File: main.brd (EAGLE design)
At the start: 50.8 x 50.8 mm, 54 parts, among them U2 SN65HVD32_D_8

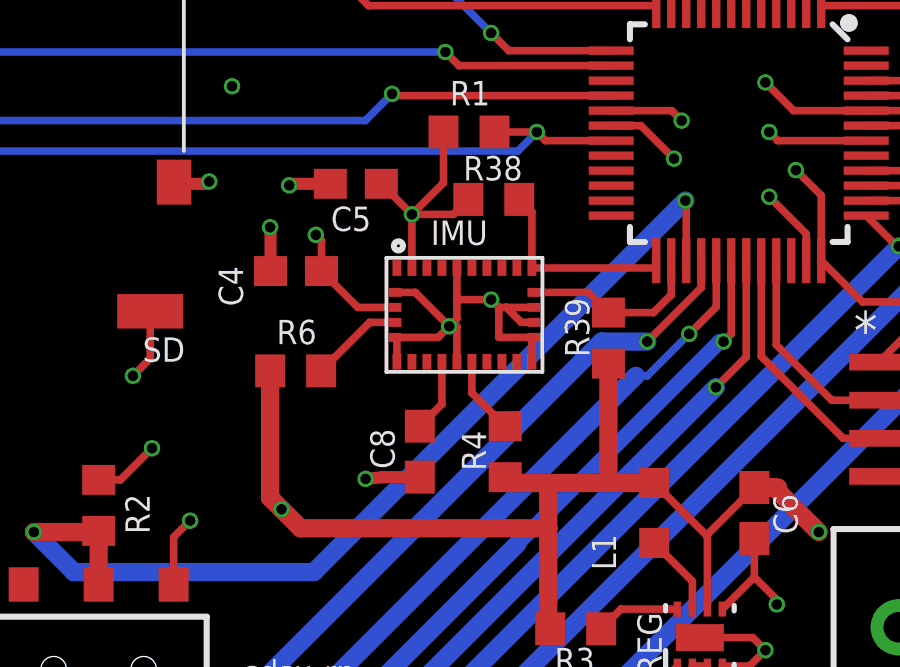
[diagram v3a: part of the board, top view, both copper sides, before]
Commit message: Fixed poly fill not connecting to all pins
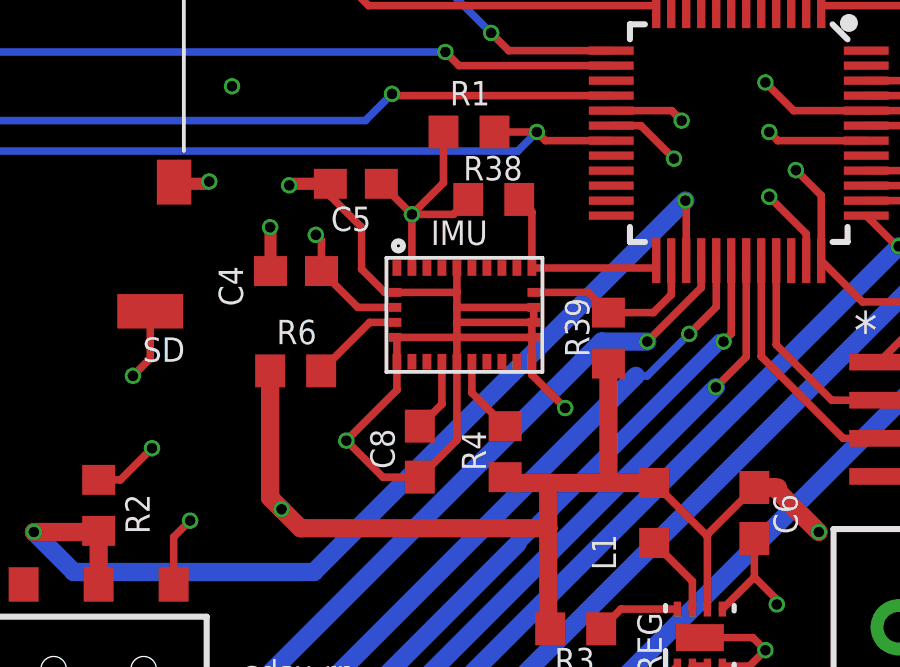
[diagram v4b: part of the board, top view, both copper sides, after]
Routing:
- net GND: track 80.3 -> 98.2 mm, vias 41 -> 40

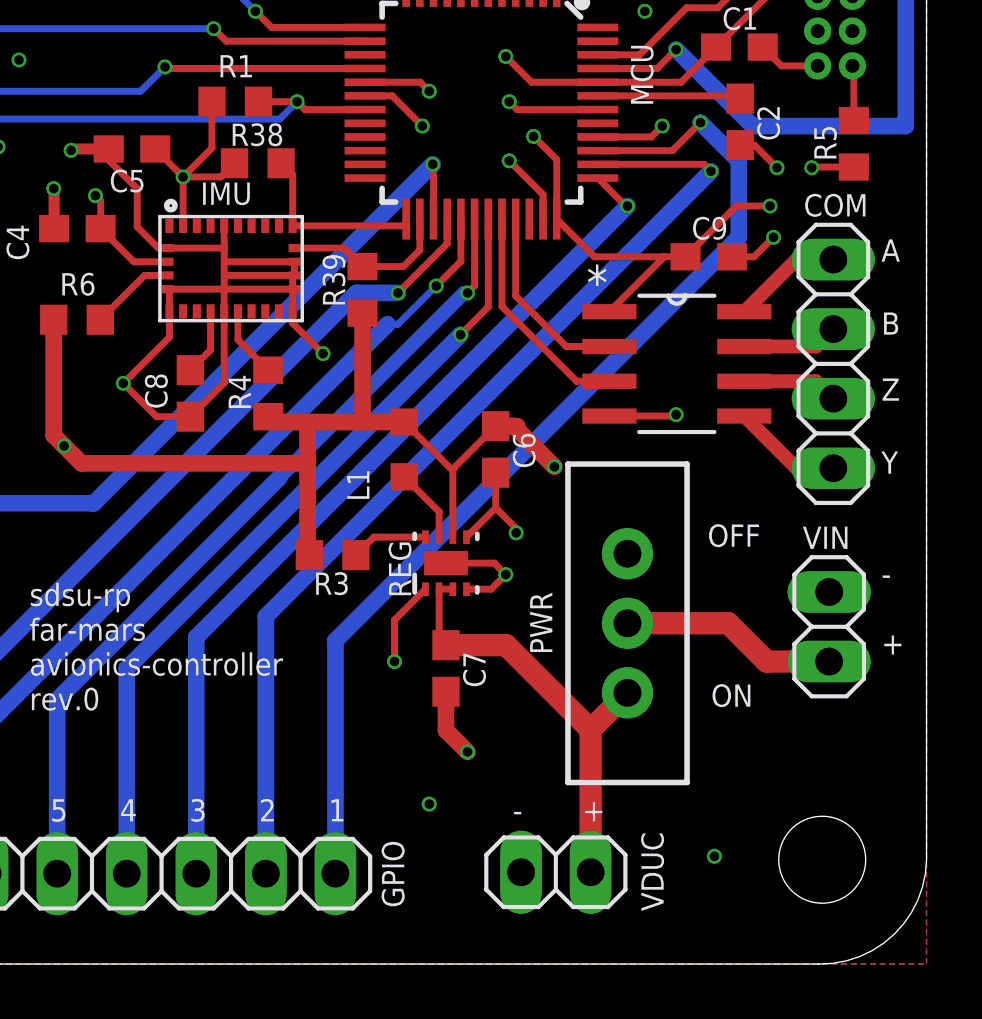
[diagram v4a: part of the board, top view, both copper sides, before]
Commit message: Changed coms transceiver, and updated documentation
Also updated bill of materials
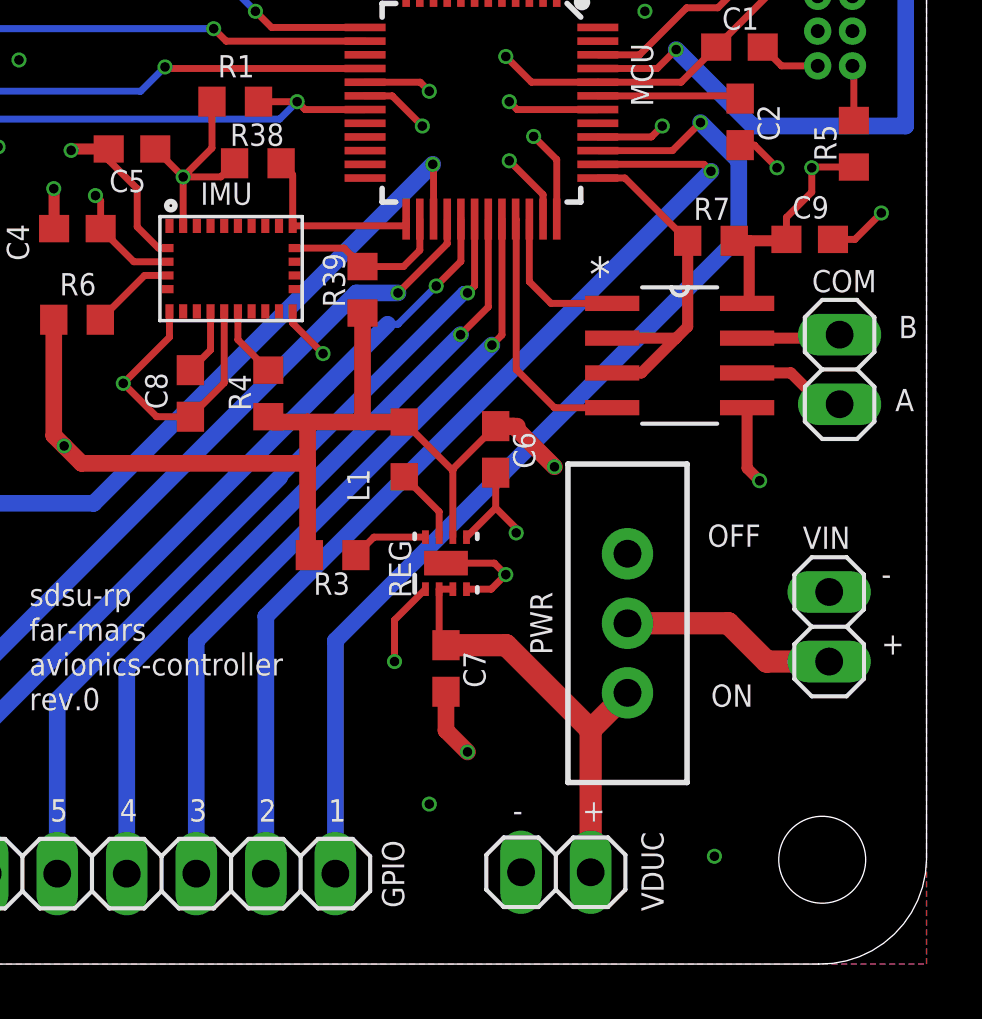
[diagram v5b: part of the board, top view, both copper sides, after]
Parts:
- removed U2: SN65HVD32_D_8, SN65HVD32:D8
- added R7: 10k, resistor:R0603
- added U1: SN65HVD10_D_8, half-dup-485:D8
- COM: device pinhead:1X04 -> pinhead:1X02
- moved C9 3.74 mm to (46.5, 26.5)
- moved COM 0.31 mm to (47.6, 21.7)
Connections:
- removed net Y: COM.4, U2.5
- removed net Z: COM.3, U2.6
- new net DATA_DIR: MCU.37, R7.2, U1.2, U1.3
- net 3.3V: now also R7.1, U1.8; no longer U2.1
- net A: now also COM.2, U1.6; no longer COM.1, U2.8
- net B: now also COM.1, U1.7; no longer COM.2, U2.7
- net GND: now also U1.5; no longer U2.4
- net GPIO3: now also MCU.32; no longer MCU.37
- net MCU_RX: now also MCU.34, U1.1; no longer MCU.32, U2.3
- net MCU_TX: now also U1.4; no longer U2.2
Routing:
- net GND: track 98.2 -> 81.3 mm
- net DATA_DIR: track 0.00 -> 13.2 mm
- net 3.3V: track 117.6 -> 112.9 mm, vias 17 -> 16
- net Y: track 4.04 -> 0.00 mm
- net GPIO3: track 32.4 -> 28.5 mm
- net Z: track 3.51 -> 0.00 mm
- net MCU_RX: track 8.25 -> 5.64 mm
- net MCU_TX: track 6.99 -> 9.58 mm
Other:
- board text removed: "Y"
- board text removed: "Z"

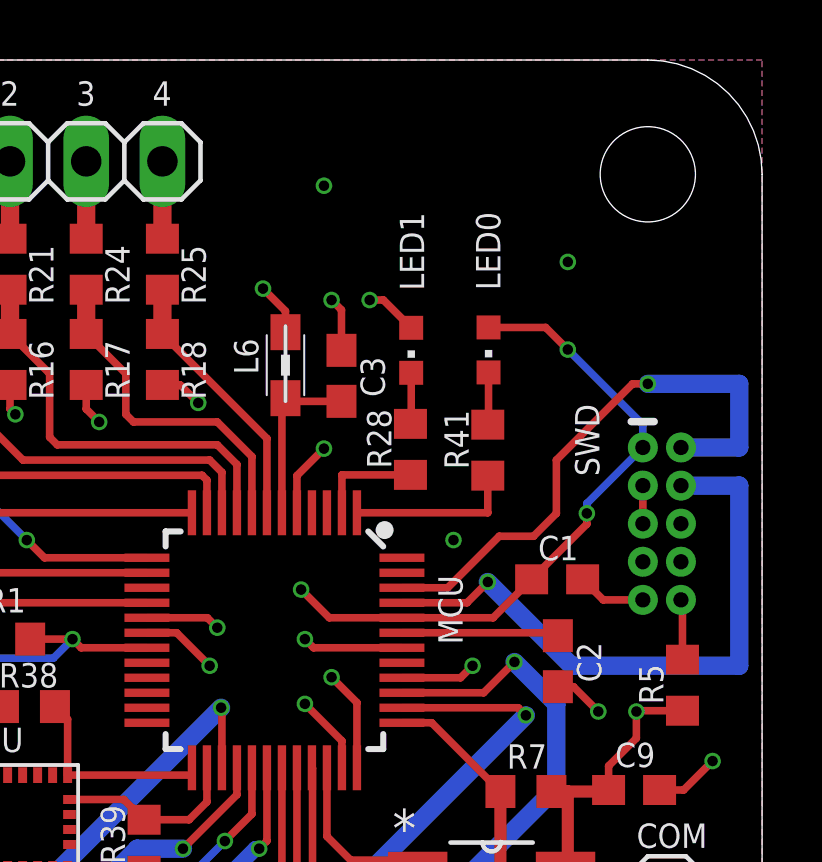
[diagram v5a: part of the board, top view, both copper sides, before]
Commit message: Switched out SWD header for one with bigger drills
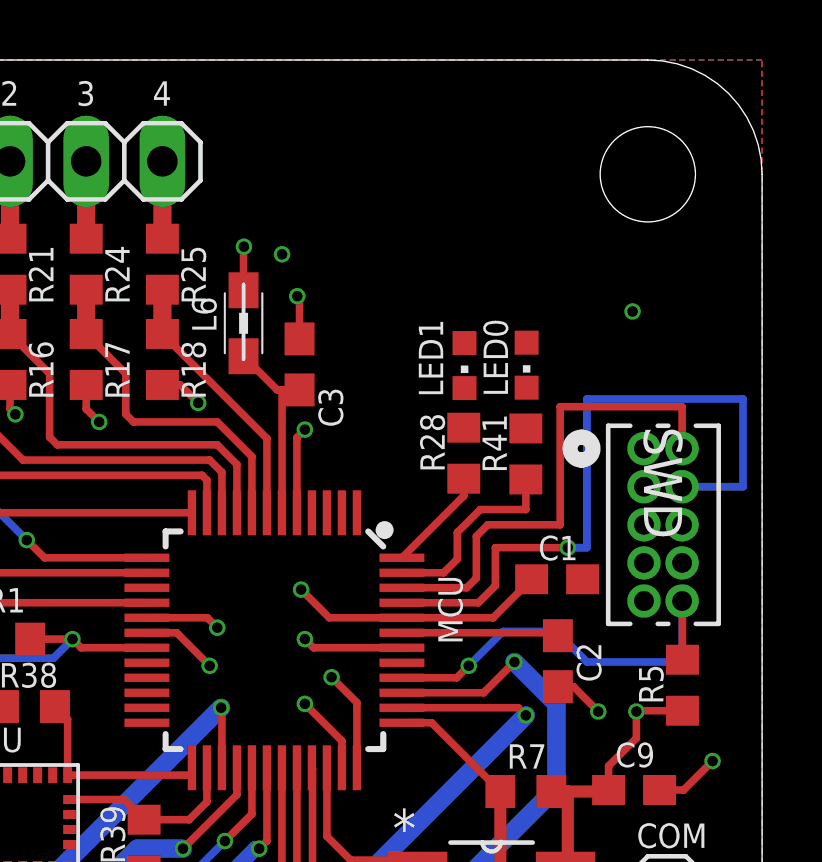
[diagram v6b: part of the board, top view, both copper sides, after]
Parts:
- SWD: value CORTEX_DEBUG_PTH -> DEBUG-HEADER; device SparkFun-Connectors:2X5-PTH-1.27MM -> senior-design-custom:CONN_MINITEK_2X5_HDR
- moved L6 1.98 mm to (33.5, 42.0)
- moved LED1 1.85 mm to (40.9, 40.6)
- moved R28 1.78 mm to (40.9, 37.7)
- moved C3 1.45 mm to (35.4, 40.7)
- moved LED0 1.37 mm to (43.0, 40.6)
- moved R41 1.28 mm to (42.9, 37.7)
- moved SWD 0.05 mm to (47.5, 35.3)
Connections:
- net PA30_SWCLK renamed SWCLK
- net PA31_SWDIO renamed SWDIO
- net SWD_NRES renamed MCU_NRST
- removed net N$14: MCU.2, R28.1
- removed net N$16: MCU.1, R41.1
- new net LED0: MCU.47, R41.1
- new net LED1: MCU.48, R28.1
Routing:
- net 3.3V: track 112.9 -> 97.7 mm, vias 16 -> 13
- net LED0: track 0.00 -> 6.53 mm
- net N$16: track 5.60 -> 0.00 mm
- net GND: track 81.3 -> 77.8 mm, vias 40 -> 39
- net N$14: track 3.55 -> 0.00 mm
- net LED1: track 0.00 -> 3.49 mm
- net SWDIO: track 19.2 -> 16.4 mm, vias 1 -> 0
- net SWCLK: track 20.6 -> 22.8 mm
- net N$7: track 1.75 -> 0.00 mm
- net N$20: track 1.71 -> 0.00 mm
- net MCU_NRST: track 12.6 -> 14.2 mm
- net N$2: track 5.78 -> 6.43 mm
